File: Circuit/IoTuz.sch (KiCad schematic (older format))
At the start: 31 parts, among them P2 BATTERY, P3 USB_5PIN_SHELL, P4 LED_1, P5 LED_2, P6 CONN_01X20, P7 CONN_01X20, Q1 S8050, Q2 S8050, Q3 FDN340P, SW3 PRGM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

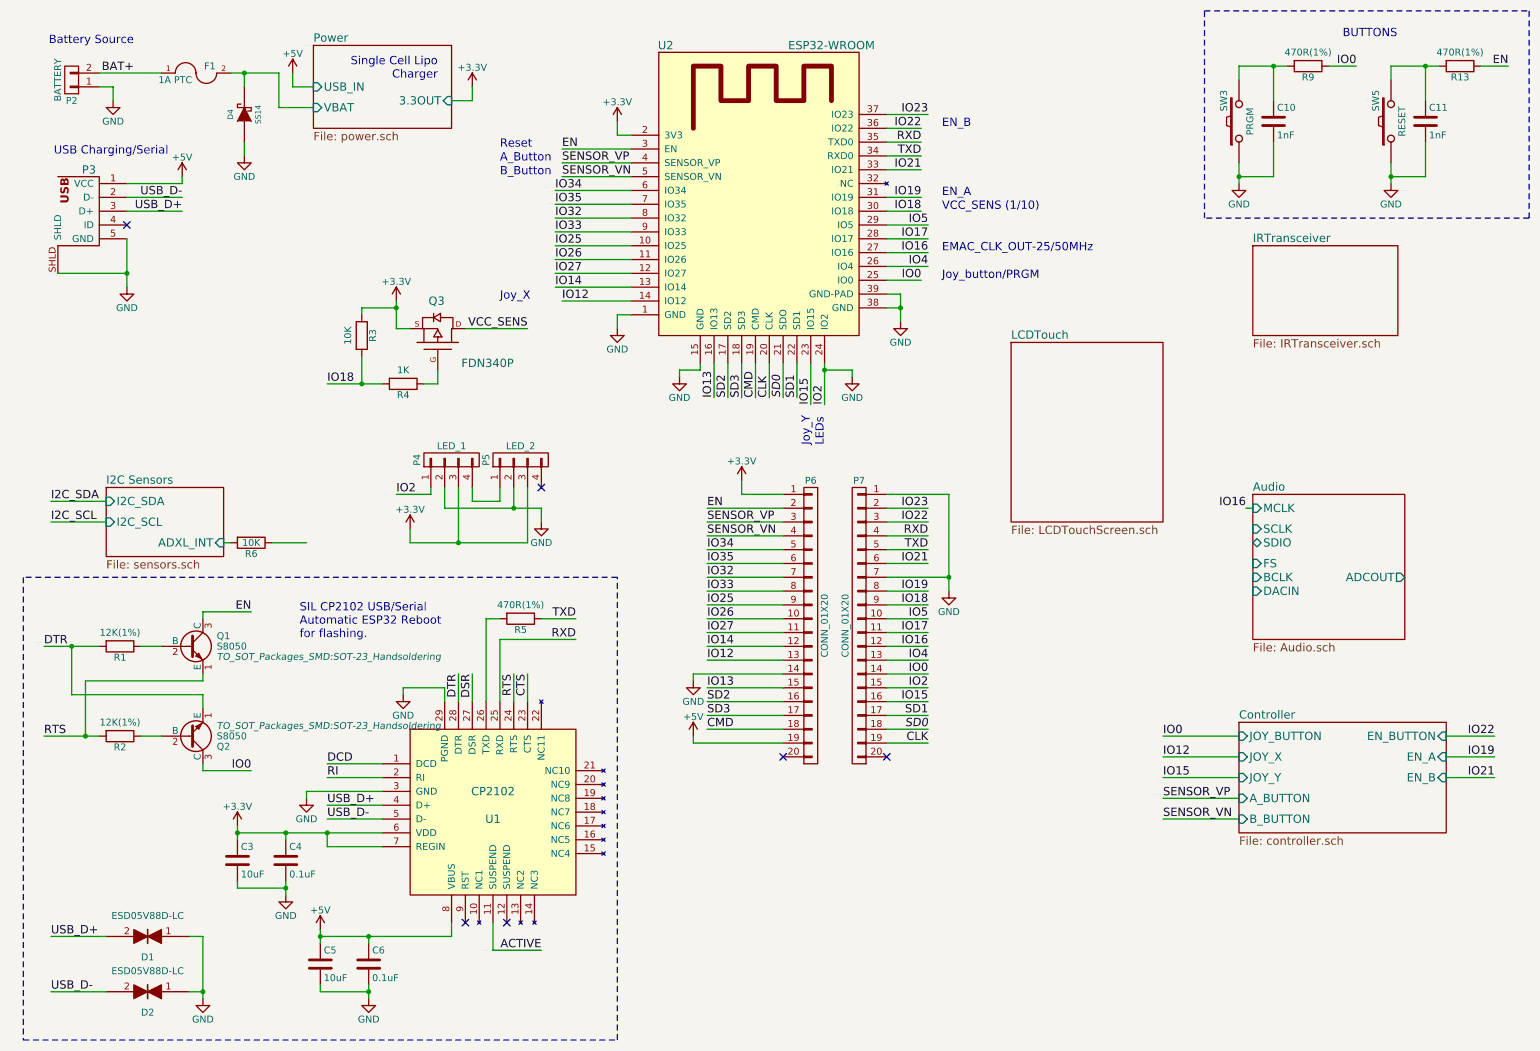
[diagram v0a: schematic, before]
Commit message: Added Alligator clip points.
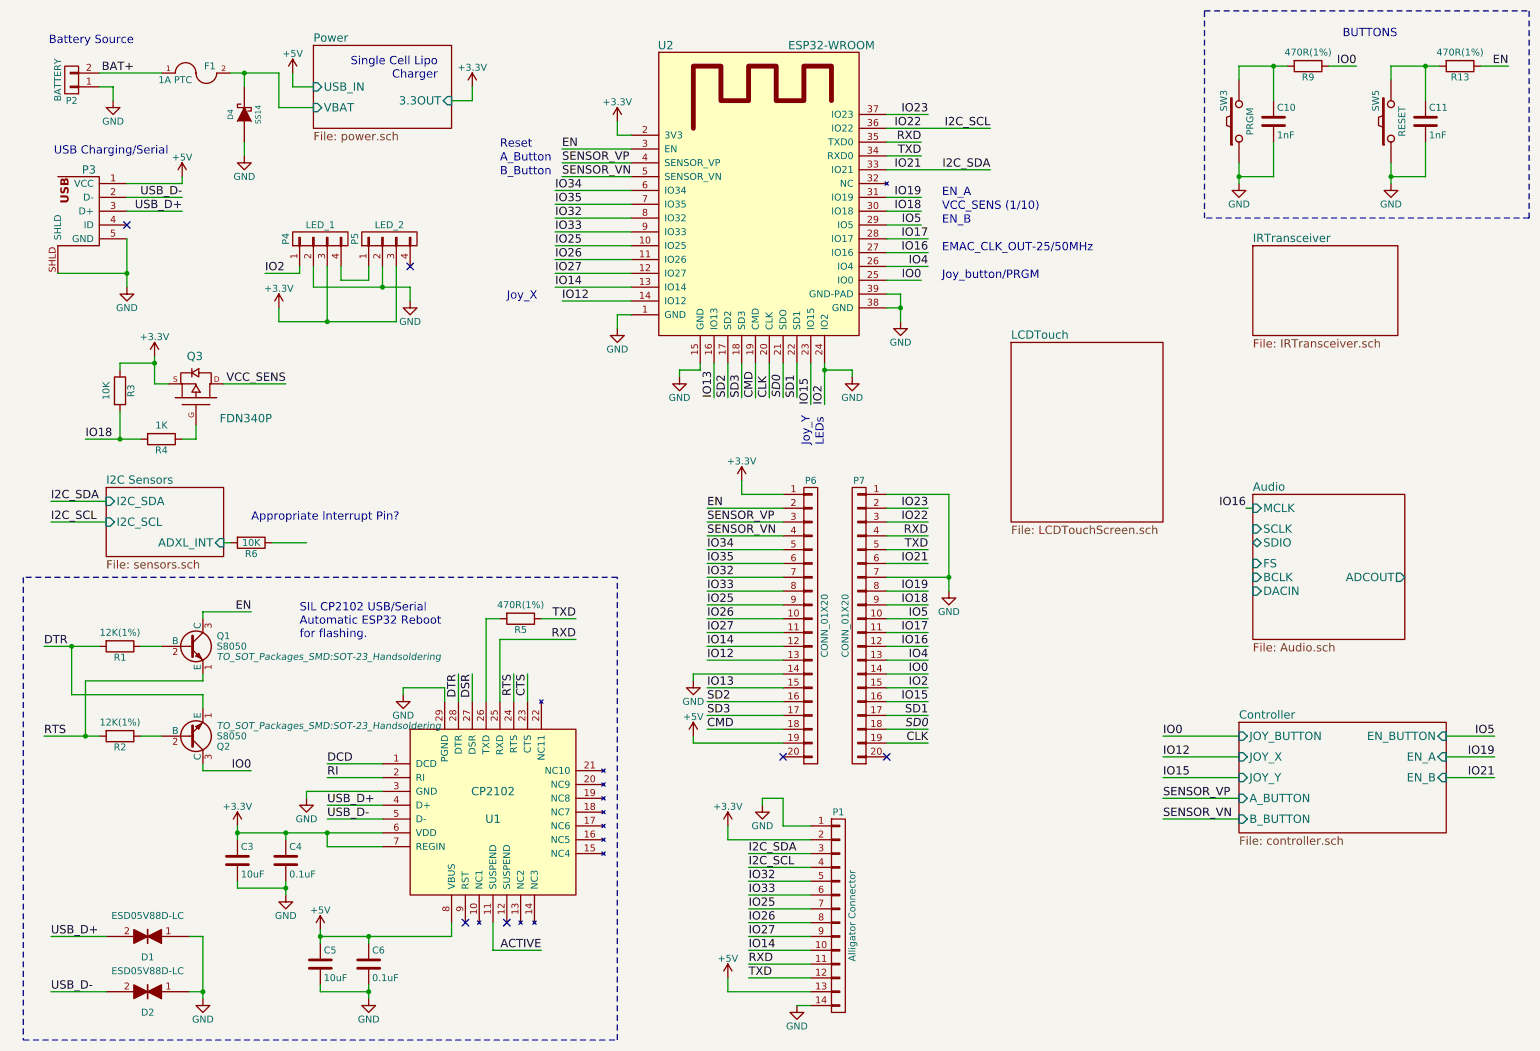
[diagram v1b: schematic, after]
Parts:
- added P1: Alligator Connector, libs:aligator_pads, symbol CONN_01X14
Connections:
- net IO21 is gone; now on net I2C_SDA: P7.6 (P6), U2.33 (IO21)
- net IO22 is gone; now on net I2C_SCL: P7.3 (P3), U2.36 (IO22)
- net +3V3: now also P1.2 (P2)
- net +5V: now also P1.13 (P13)
- net GND: now also P1.1 (P1), P1.14 (P14)
- net I2C_SCL: now also P1.4 (P4)
- net I2C_SDA: now also P1.3 (P3)
- net IO14: now also P1.10 (P10)
- net IO25: now also P1.7 (P7)
- net IO26: now also P1.8 (P8)
- net IO27: now also P1.9 (P9)
- net IO32: now also P1.5 (P5)
- net IO33: now also P1.6 (P6)
- net RXD: now also P1.11 (P11)
- net TXD: now also P1.12 (P12)
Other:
- note added: "Appropriate Interrupt Pin?"
- moved on the sheet: P4, P5, Q3, R3, R4

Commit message: IRTx & forward slashing the fp-lib-table.
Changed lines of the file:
@@
 $EndSheet
 $Sheet
-S 9300 2100 1050 650
+S 9300 2100 1050 300
 U 5811E5C9
 F0 "IRTransceiver" 60
 F1 "IRTransceiver.sch" 60
+F2 "IRRx" O R 10350 2250 60
+F3 "IRTx" I L 9300 2250 60
 $EndSheet
 Text Notes 7050 2350 0    60   ~ 0

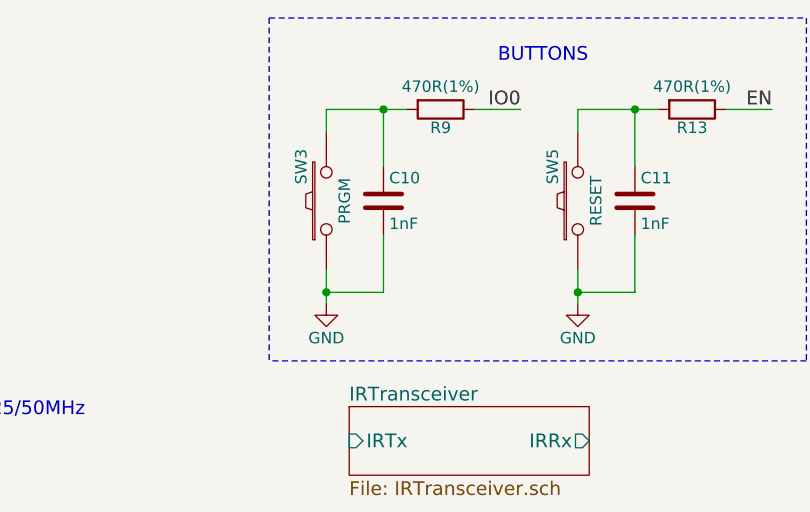
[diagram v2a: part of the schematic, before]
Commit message: Removed PRGM button. placed some components.
PGRM button can be performed by joystick.
CHRG led removed.
placed some components.
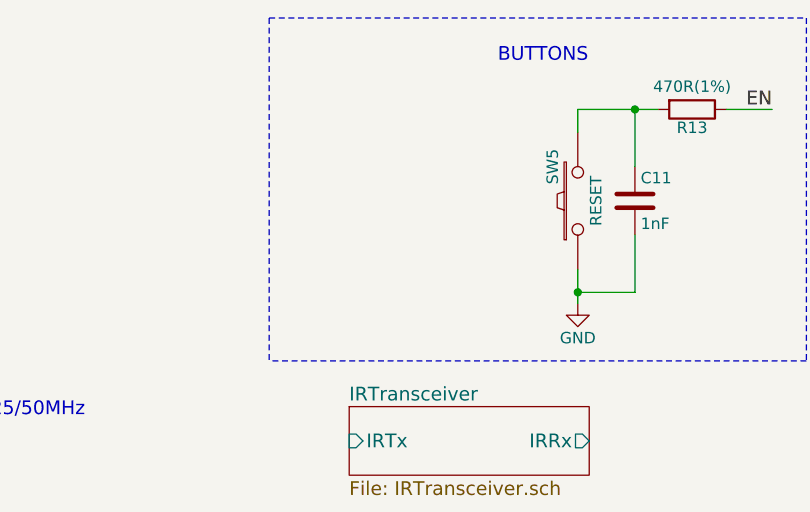
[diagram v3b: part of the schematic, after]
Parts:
- removed C10: 1nF, Capacitors_SMD:C_0603_HandSoldering, symbol C
- removed R9: 470R(1%), Resistors_SMD:R_0603_HandSoldering, symbol R
- removed SW3: PRGM, freetronics_footprints:SW_PUSHBUTTON_PTH, symbol SW_PUSH
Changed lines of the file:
@@
 $Comp
 L GND #PWR016
-U 1 1 580858E3
-P 9200 1650
-F 0 "#PWR016" H 9200 1400 50  0001 C CNN
-F 1 "GND" H 9200 1500 50  0000 C CNN
-F 2 "" H 9200 1650 50  0000 C CNN
-F 3 "" H 9200 1650 50  0000 C CNN
-	1    9200 1650
-	1    0    0    -1
-$EndComp
-$Comp
-L SW_PUSH SW3
-U 1 1 5808593D
-P 9200 1200
-F 0 "SW3" H 9350 1310 50  0000 C CNN
-F 1 "PRGM" H 9200 1120 50  0000 C CNN
-F 2 "freetronics_footprints:SW_PUSHBUTTON_PTH" H 9200 1200 50  0001 C CNN
-F 3 "" H 9200 1200 50  0000 C CNN
-	1    9200 1200
-	0    -1   -1   0
-$EndComp
-$Comp
-L R R9
-U 1 1 58085AAD
-P 9700 800
-F 0 "R9" V 9780 800 50  0000 C CNN
-F 1 "470R(1%)" V 9600 800 50  0000 C CNN
-F 2 "Resistors_SMD:R_0603_HandSoldering" V 9630 800 50  0001 C CNN
-F 3 "" H 9700 800 50  0000 C CNN
-	1    9700 800
-	0    1    1    0
-$EndComp
-$Comp
-L C C10
-U 1 1 58085F33
-P 9450 1200
-F 0 "C10" H 9475 1300 50  0000 L CNN
-F 1 "1nF" H 9475 1100 50  0000 L CNN
-F 2 "Capacitors_SMD:C_0603_HandSoldering" H 9488 1050 50  0001 C CNN
-F 3 "" H 9450 1200 50  0000 C CNN
-	1    9450 1200
-	1    0    0    -1
-$EndComp
-Text Label 10050 800  2    60   ~ 0
-IO0
-$Comp
-L GND #PWR017
 U 1 1 58086D5A
 P 10300 1650
-F 0 "#PWR017" H 10300 1400 50  0001 C CNN
+F 0 "#PWR016" H 10300 1400 50  0001 C CNN
 F 1 "GND" H 10300 1500 50  0000 C CNN
 F 2 "" H 10300 1650 50  0000 C CNN
@@
 IO0
 $Comp
-L GND #PWR018
+L GND #PWR017
 U 1 1 5809017E
 P 6400 3050
-F 0 "#PWR018" H 6400 2800 50  0001 C CNN
+F 0 "#PWR017" H 6400 2800 50  0001 C CNN
 F 1 "GND" H 6400 2900 50  0000 C CNN
 F 2 "" H 6400 3050 50  0000 C CNN
@@
 NoConn ~ 3200 2250
 $Comp
-L +3.3V #PWR019
+L +3.3V #PWR018
 U 1 1 580DAAD9
 P 2250 2550
-F 0 "#PWR019" H 2250 2400 50  0001 C CNN
+F 0 "#PWR018" H 2250 2400 50  0001 C CNN
 F 1 "+3.3V" H 2250 2690 50  0000 C CNN
 F 2 "" H 2250 2550 50  0000 C CNN
@@
 $EndComp
 $Comp
-L GND #PWR020
+L GND #PWR019
 U 1 1 580DAB83
 P 3200 2500
-F 0 "#PWR020" H 3200 2250 50  0001 C CNN
+F 0 "#PWR019" H 3200 2250 50  0001 C CNN
 F 1 "GND" H 3200 2350 50  0000 C CNN
 F 2 "" H 3200 2500 50  0000 C CNN
@@
 $EndComp
 $Comp
-L +3.3V #PWR021
+L +3.3V #PWR020
 U 1 1 580E52A3
 P 1350 2900
-F 0 "#PWR021" H 1350 2750 50  0001 C CNN
+F 0 "#PWR020" H 1350 2750 50  0001 C CNN
 F 1 "+3.3V" H 1350 3040 50  0000 C CNN
 F 2 "" H 1350 2900 50  0000 C CNN
@@
 $EndComp
 $Comp
-L +3.3V #PWR022
+L +3.3V #PWR021
 U 1 1 580EDF72
 P 5600 3800
-F 0 "#PWR022" H 5600 3650 50  0001 C CNN
+F 0 "#PWR021" H 5600 3650 50  0001 C CNN
 F 1 "+3.3V" H 5600 3940 50  0000 C CNN
 F 2 "" H 5600 3800 50  0000 C CNN
@@
 IO12
 $Comp
-L GND #PWR023
+L GND #PWR022
 U 1 1 580EFC34
 P 5250 5250
-F 0 "#PWR023" H 5250 5000 50  0001 C CNN
+F 0 "#PWR022" H 5250 5000 50  0001 C CNN
 F 1 "GND" H 5250 5100 50  0000 C CNN
 F 2 "" H 5250 5250 50  0000 C CNN
@@
 CMD
 $Comp
-L +5V #PWR024
+L +5V #PWR023
 U 1 1 580F08CD
 P 5250 5650
-F 0 "#PWR024" H 5250 5500 50  0001 C CNN
+F 0 "#PWR023" H 5250 5500 50  0001 C CNN
 F 1 "+5V" H 5250 5790 50  0000 C CNN
 F 2 "" H 5250 5650 50  0000 C CNN
@@
 $EndComp
 $Comp
-L GND #PWR025
+L GND #PWR024
 U 1 1 580F2337
 P 7100 4600
-F 0 "#PWR025" H 7100 4350 50  0001 C CNN
+F 0 "#PWR024" H 7100 4350 50  0001 C CNN
 F 1 "GND" H 7100 4450 50  0000 C CNN
 F 2 "" H 7100 4600 50  0000 C CNN
@@
 CLK
 $Comp
-L +5V #PWR026
+L +5V #PWR025
 U 1 1 58114717
 P 1550 1600
-F 0 "#PWR026" H 1550 1450 50  0001 C CNN
+F 0 "#PWR025" H 1550 1450 50  0001 C CNN
 F 1 "+5V" H 1550 1740 50  0000 C CNN
 F 2 "" H 1550 1600 50  0000 C CNN
@@
 $EndComp
 $Comp
-L +5V #PWR027
+L +5V #PWR026
 U 1 1 581147C2
 P 2350 850
-F 0 "#PWR027" H 2350 700 50  0001 C CNN
+F 0 "#PWR026" H 2350 700 50  0001 C CNN
 F 1 "+5V" H 2350 990 50  0000 C CNN
 F 2 "" H 2350 850 50  0000 C CNN
@@
 $EndComp
 $Comp
-L +3.3V #PWR028
+L +3.3V #PWR027
 U 1 1 581DAACE
 P 5500 6300
-F 0 "#PWR028" H 5500 6150 50  0001 C CNN
+F 0 "#PWR027" H 5500 6150 50  0001 C CNN
 F 1 "+3.3V" H 5500 6440 50  0000 C CNN
 F 2 "" H 5500 6300 50  0000 C CNN
@@
 $EndComp
 $Comp
-L GND #PWR029
+L GND #PWR028
 U 1 1 581DB8B4
 P 5750 6150
-F 0 "#PWR029" H 5750 5900 50  0001 C CNN
+F 0 "#PWR028" H 5750 5900 50  0001 C CNN
 F 1 "GND" H 5750 6000 50  0000 C CNN
 F 2 "" H 5750 6150 50  0000 C CNN
@@
 $EndComp
 $Comp
-L GND #PWR030
+L GND #PWR029
 U 1 1 581DC5E9
 P 6000 7600
-F 0 "#PWR030" H 6000 7350 50  0001 C CNN
+F 0 "#PWR029" H 6000 7350 50  0001 C CNN
 F 1 "GND" H 6000 7450 50  0000 C CNN
 F 2 "" H 6000 7600 50  0000 C CNN
@@
 $EndComp
 $Comp
-L +5V #PWR031
+L +5V #PWR030
 U 1 1 581DCC5D
 P 5500 7400
-F 0 "#PWR031" H 5500 7250 50  0001 C CNN
+F 0 "#PWR030" H 5500 7250 50  0001 C CNN
 F 1 "+5V" H 5500 7540 50  0000 C CNN
 F 2 "" H 5500 7400 50  0000 C CNN
@@
 	4700 7850 4700 4500
 Wire Wire Line
-	9200 900  9200 800
-Wire Wire Line
-	9200 800  9550 800
-Wire Wire Line
-	9450 1050 9450 800
-Connection ~ 9450 800
-Wire Wire Line
-	9200 1500 9200 1650
-Wire Wire Line
-	9200 1600 9450 1600
-Wire Wire Line
-	9450 1600 9450 1350
-Connection ~ 9200 1600
-Wire Wire Line
-	9850 800  10050 800
-Wire Wire Line
 	10300 900  10300 800
